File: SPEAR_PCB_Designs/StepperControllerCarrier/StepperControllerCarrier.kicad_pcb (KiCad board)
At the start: 2 copper layers, 109 x 49 mm, 19 parts, among them J1 Conn_01x02_Pin, J2 Conn_01x02_Pin, J3 Conn_01x02_Pin, J4 Conn_01x02_Pin, J5 Conn_01x04_Pin, U1 AP63203WU

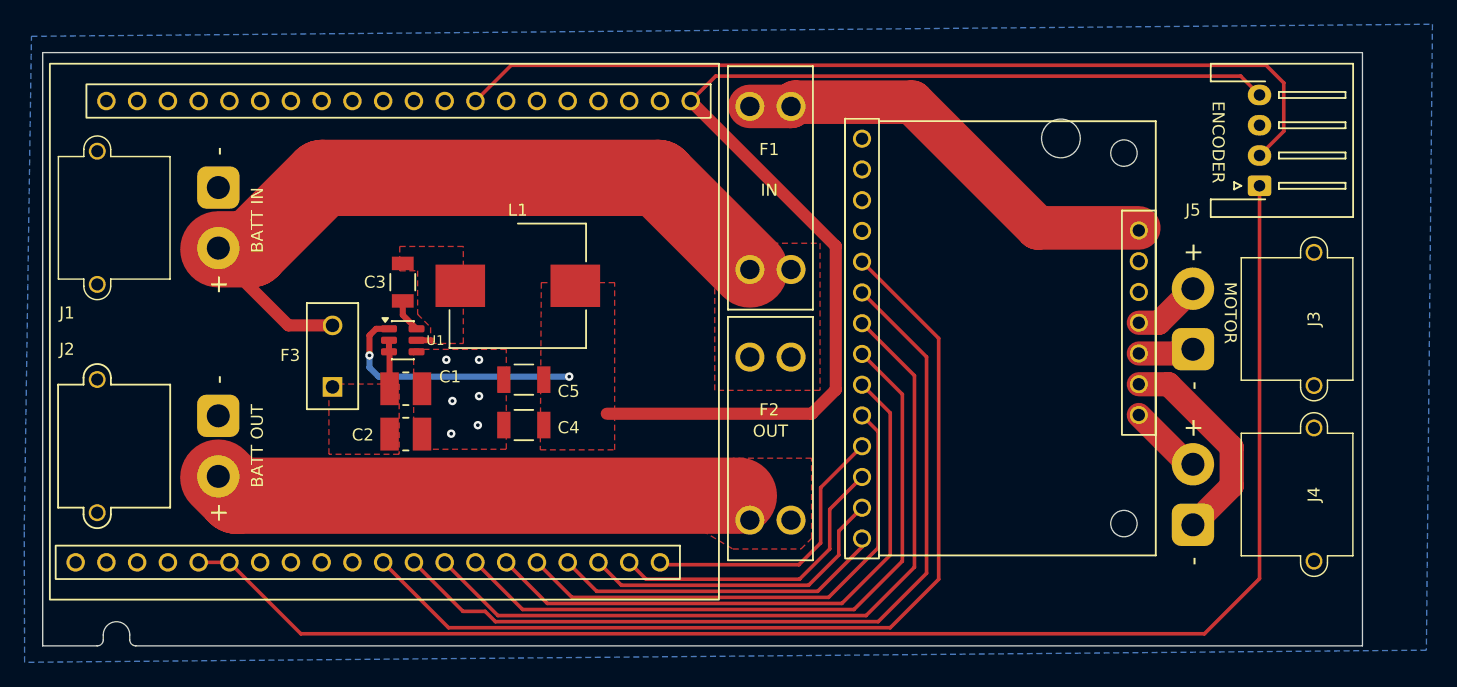
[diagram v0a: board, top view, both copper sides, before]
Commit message: Moved mounting hole on stepper controller carrier
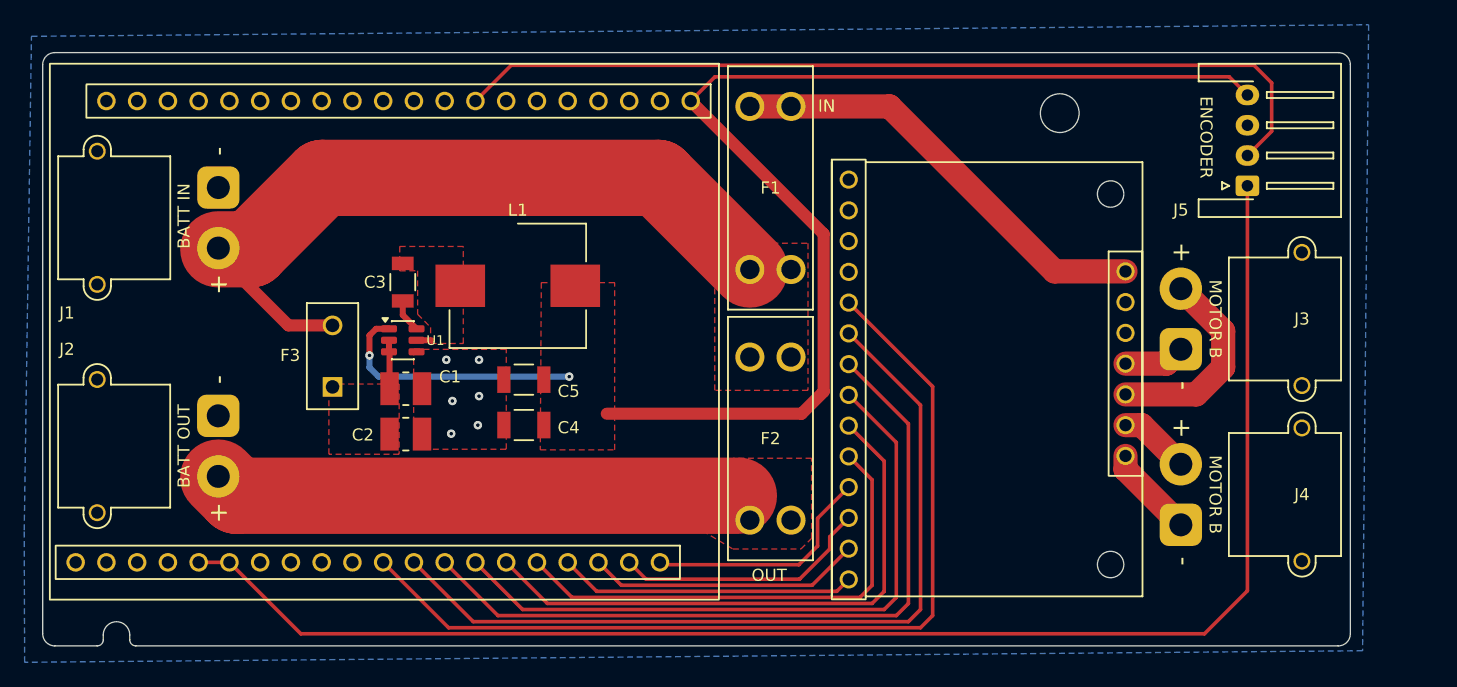
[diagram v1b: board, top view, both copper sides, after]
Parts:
- F1: value 10 A -> 10A
- J1, J3, J4: footprint Connector_AMASS:AMASS_XT30PW-M_1x02_P2.50mm_Horizontal -> SPEAR_Connectors:AMASS_XT30PW-M_1x02_P2.50mm_Horizontal_1
- moved MDB1 3.55 mm to (153.3, 81.2)
- moved REF** 2.09 mm to (172.0, 77.0)
- moved J3 1.00 mm to (182.0, 96.5)
- moved J4 1.00 mm to (182.0, 111.0)
- moved J5 1.00 mm to (187.5, 83.0)
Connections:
- MDB1 pad 18: Net-(J3-Pin_2) -> Net-(J3-Pin_1)
- MDB1 pad 19: Net-(J3-Pin_1) -> Net-(J3-Pin_2)
- MDB1 pad 20: Net-(J4-Pin_1) -> Net-(J4-Pin_2)
- MDB1 pad 21: Net-(J4-Pin_2) -> Net-(J4-Pin_1)
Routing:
- net Net-(J3-Pin_2): track 5.63 -> 16.9 mm
- net Net-(J4-Pin_1): track 17.6 -> 7.58 mm
- net /MO: track 25.2 -> 21.4 mm
- net /RESET: track 23.5 -> 19.7 mm
- net /LO1: track 26.4 -> 22.7 mm
- net /LO2: track 27.5 -> 24.6 mm
- net +3.3V: track 118.3 -> 115.9 mm
- net /DMODE0: track 78.6 -> 76.8 mm
- net /DMODE2: track 64.2 -> 62.3 mm
- net /STEP: track 49.8 -> 47.9 mm
- net /DIR: track 57.0 -> 55.1 mm
- net /DMODE1: track 71.4 -> 69.5 mm
- net /ENABLE: track 42.6 -> 40.7 mm
- net /ENC_A: track 75.4 -> 74.4 mm
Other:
- board size 109 x 49 mm -> 108 x 49 mm
- board text added: "MOTOR B"
- board text removed: "MOTOR"
